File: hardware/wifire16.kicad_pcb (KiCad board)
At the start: 2 copper layers, 203.2 x 82.5 mm, 164 parts, among them M1 XBEE-PRO, P1 SOL1, P10 SOL10, P11 SOL11, P12 SOL12, P13 SOL13, P14 SOL14, P15 SOL15, P16 SOL16, P17 SOLPWR, P18 TLC IN, P19 TLC OUT, P2 SOL2, P20 TTL-232R, P21 ICSP, P22 XBEE_1, P23 XBEE_2, P24 PORTC, P25 PORTD, P26 PORTB, P27 POWER, P3 SOL3, P4 SOL4, P5 SOL5, P6 SOL6, P7 SOL7, P8 SOL8, P9 SOL9, Q1 IRF510, Q10 IRF510, Q11 IRF510, Q12 IRF510, Q13 IRF510, Q14 IRF510, Q15 IRF510, Q16 IRF510, Q2 IRF510, Q3 IRF510, Q4 IRF510, Q5 IRF510, Q6 IRF510, Q7 IRF510, Q8 IRF510, Q9 IRF510, SW1 RESET, U1 4N35, U10 4N35, U11 4N35, U12 4N35, U13 4N35, U14 4N35, U15 4N35, U16 4N35, U17 4N35, U18 TLC5940, U19 MCP1700 3V3, U2 4N35, U20 74AHC125, U21 LM7805, U22 ATMEGA328, U23 MCP1702 1V5, U3 4N35, U4 4N35, U5 4N35, U6 4N35, U7 4N35, U8 4N35, U9 4N35, Y1 16MHz

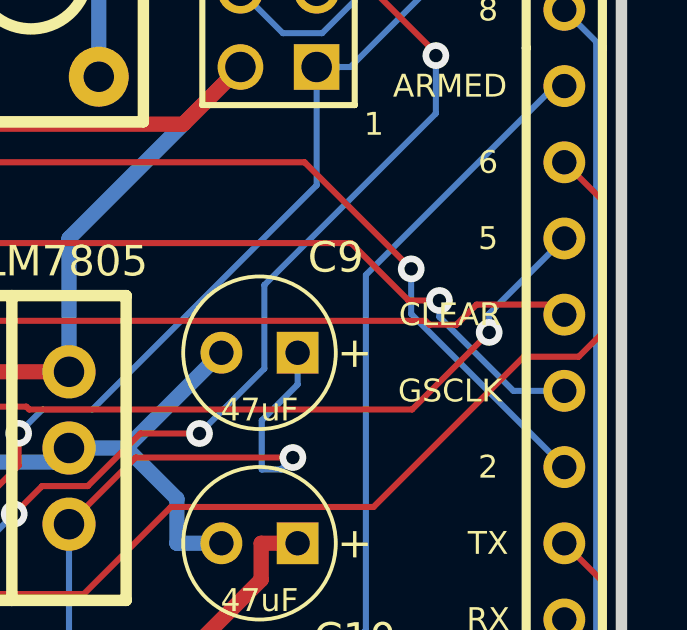
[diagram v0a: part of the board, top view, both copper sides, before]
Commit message: removing unused pin name
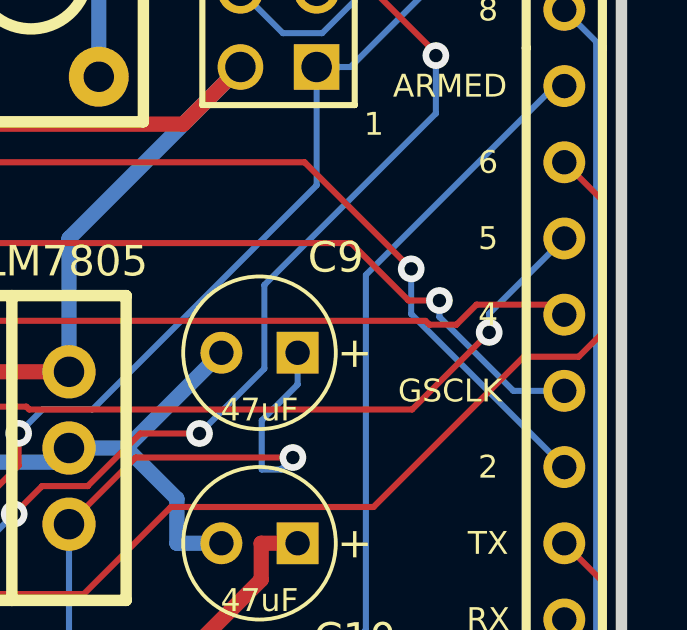
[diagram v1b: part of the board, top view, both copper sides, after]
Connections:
- net /CLEAR renamed Net-(P25-Pad5)
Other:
- board text added: "4"
- board text removed: "CLEAR"
